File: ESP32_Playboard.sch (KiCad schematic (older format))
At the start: 31 parts

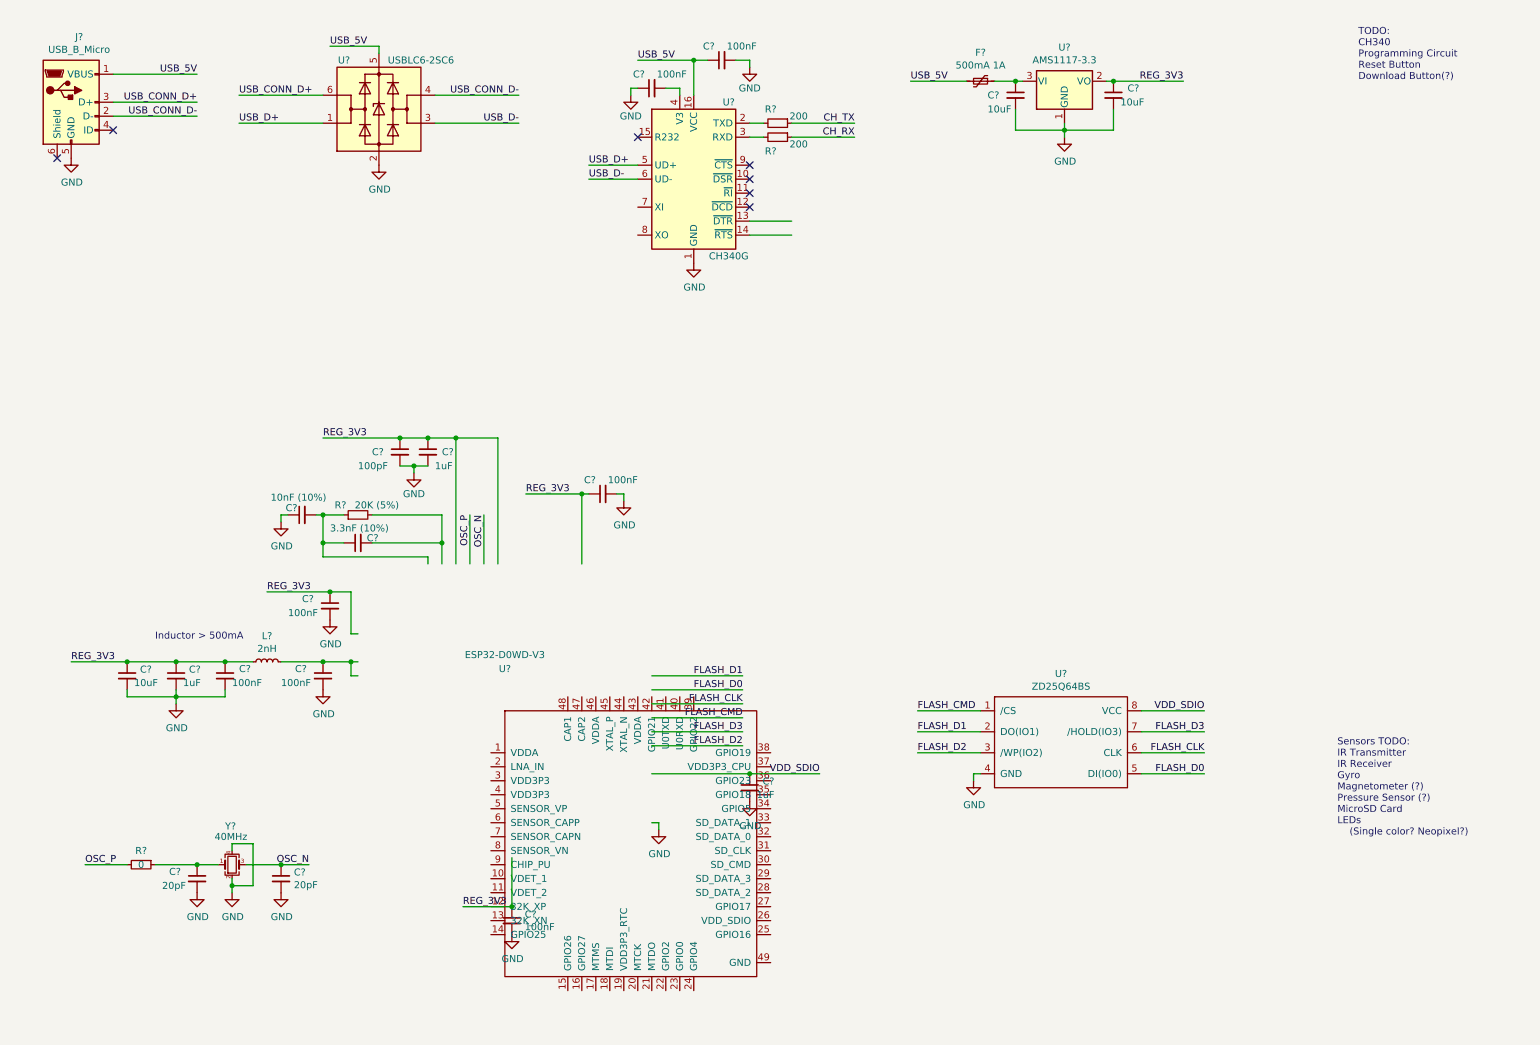
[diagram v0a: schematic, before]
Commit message: Added IR Transmitter & Receiver
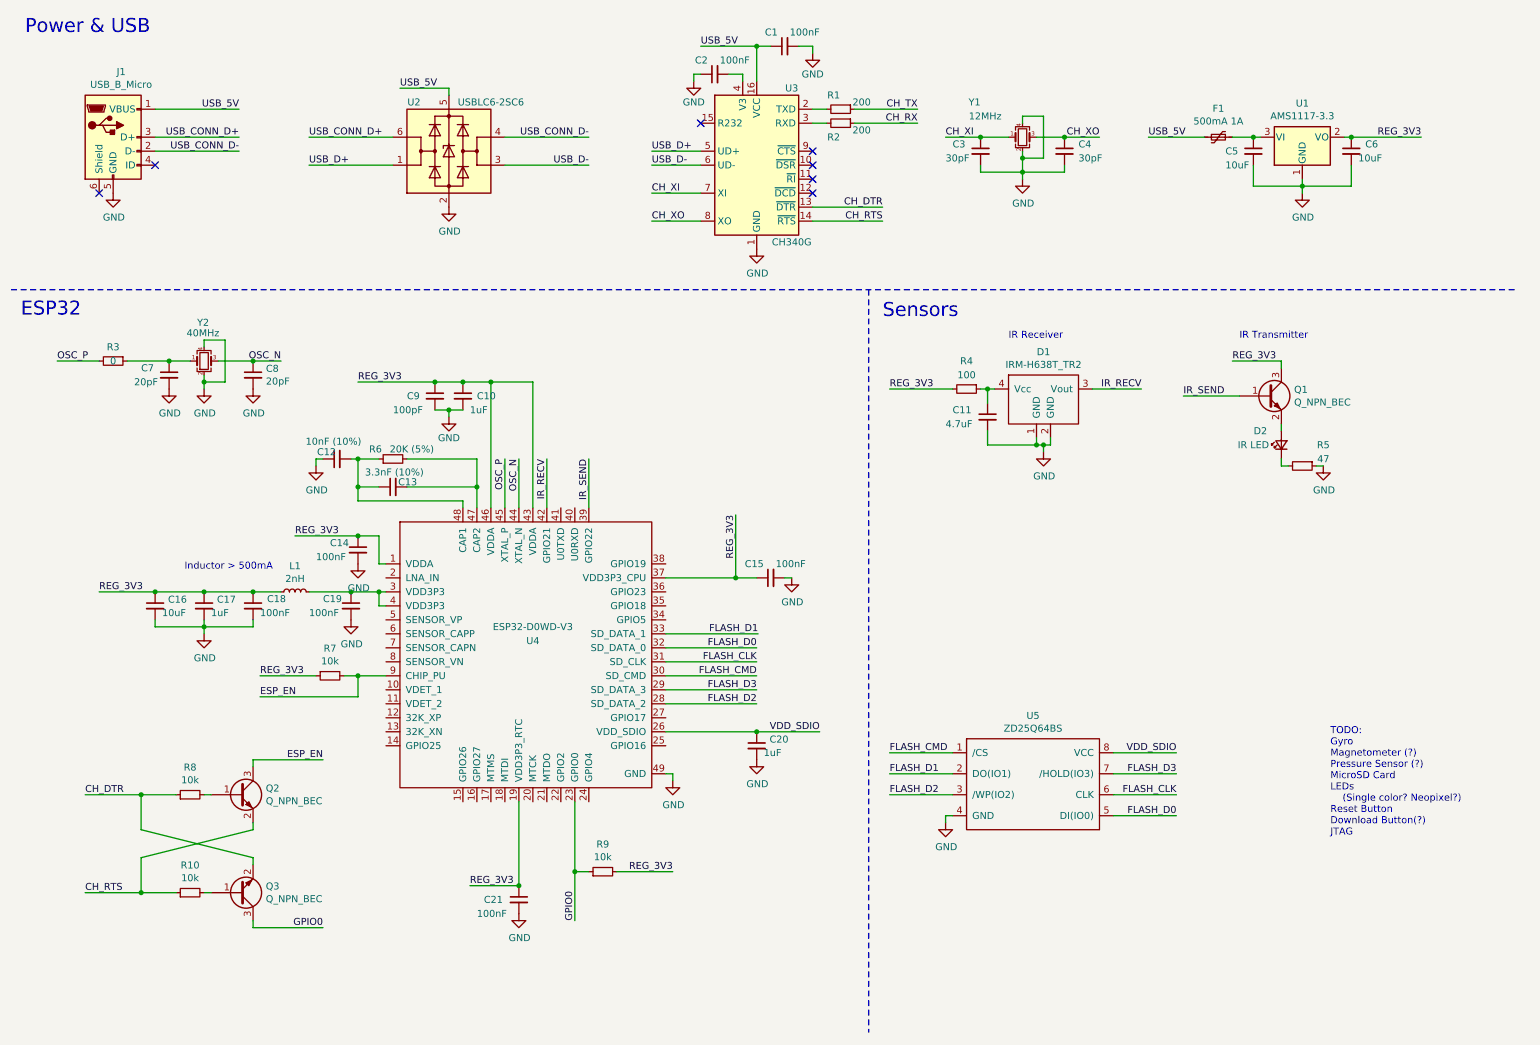
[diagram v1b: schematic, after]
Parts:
- added C11: 4.7uF, Capacitor_SMD:C_0603_1608Metric, symbol Device:C_Small
- added C3, C4: 30pF, Capacitor_SMD:C_0603_1608Metric, symbol Device:C_Small
- added D1: IRM-H638T_TR2, PlayboardLib:LED_SMD-4, symbol PlayboardLib:IRM-H638T_TR2
- added D2: IR LED, LED_SMD:LED_0603_1608Metric, symbol Device:LED_Small
- added Q1, Q2, Q3: Q_NPN_BEC, Package_TO_SOT_SMD:SOT-23, symbol Device:Q_NPN_BEC
- added R10, R7, R8, R9: 10k, Resistor_SMD:R_0603_1608Metric, symbol Device:R_Small
- added R4: 100, Resistor_SMD:R_0603_1608Metric, symbol Device:R_Small
- added R5: 47, Resistor_SMD:R_0603_1608Metric, symbol Device:R_Small
- added Y1: 12MHz, Crystal:Crystal_SMD_3225-4Pin_3.2x2.5mm, symbol Device:Crystal_GND24_Small
- C7, C8: renamed from C?; LCSC Link https://www.lcsc.com/product-detail/C326779.html -> https://www.lcsc.com/product-detail/C105621.html; LCSC Part Number C326779 -> C105621; Manufacturer Part Number CC0603FRNPO9BN200 -> CC0603JRNPO9BN200
- R1, R2: renamed from R?; footprint (none) -> Resistor_SMD:R_0603_1608Metric; LCSC Link (none) -> https://www.lcsc.com/product-detail/C25217.html; LCSC Part Number (none) -> C25217; Manufacturer (none) -> UNI-ROYAL(Uniroyal Elec); Manufacturer Part Number (none) -> 0603WAJ0201T5E
- U3: renamed from U?; LCSC Link (none) -> https://www.lcsc.com/product-detail/C14267.html; LCSC Part Number (none) -> C14267; Manufacturer (none) -> WCH(Jiangsu Qin Heng); Manufacturer Part Number (none) -> CH340G
- gave numbers to parts that had none: 26
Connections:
- net labels added: CH_DTR, CH_RTS, CH_XI, CH_XO, ESP_EN, GPIO0, IR_RECV, IR_SEND
- wire segments 117 -> 179
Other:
- note added: "ESP32"
- note added: "IR Receiver"
- note added: "IR Transmitter"
- note added: "Power & USB"
- note added: "Sensors"
- note added: "TODO:\nGyro\nMagnetometer (?)\nPressure Sensor (?)\nMicroSD Card\nLEDs\n (Single color? Neopixel?)\nReset Button\nDownload Button(?)\nJTAG\n"
- note removed: "Sensors TODO:\nIR Transmitter\nIR Receiver\nGyro\nMagnetometer (?)\nPressure Sensor (?)\nMicroSD Card\nLEDs\n (Single color? Neopixel?)\n"
- note removed: "TODO:\nCH340\nProgramming Circuit\nReset Button\nDownload Button(?)"
- moved on the sheet: C1, C10, C12, C13, C14, C15, C16, C17, C18, C19, C2, C20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

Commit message: Finished adding SD Card, IMU, Temp sensor
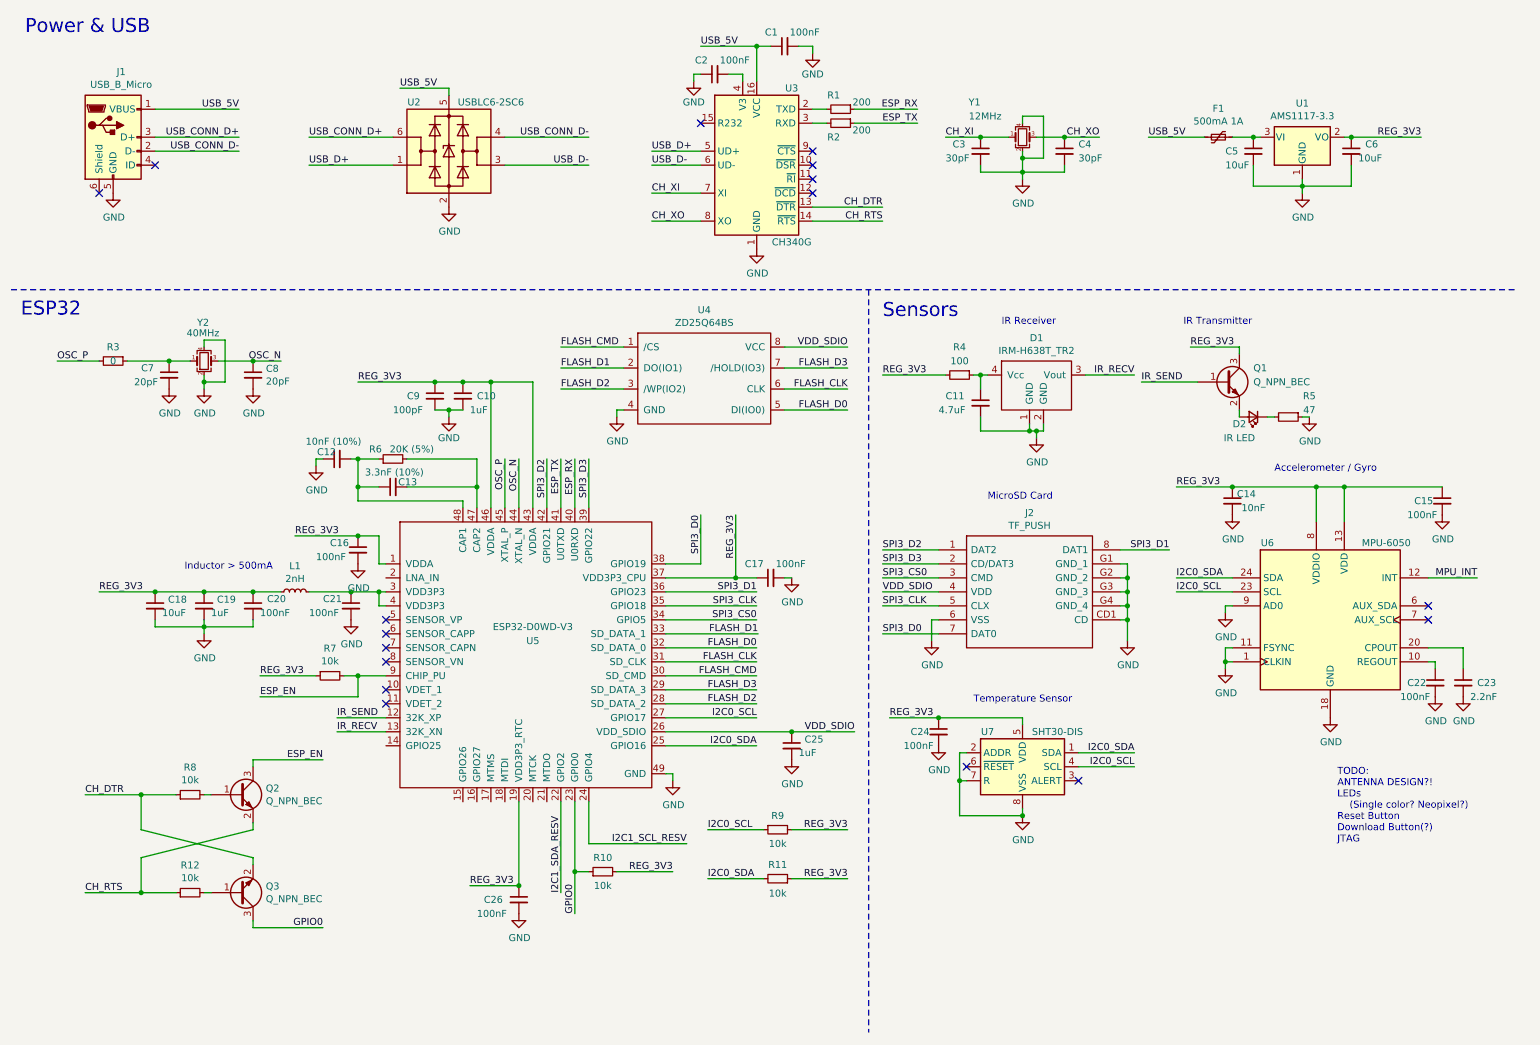
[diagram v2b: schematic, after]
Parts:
- added C14: 10nF, Capacitor_SMD:C_0603_1608Metric, symbol Device:C_Small
- added C15, C22, C24: 100nF, Capacitor_SMD:C_0603_1608Metric, symbol Device:C_Small
- added C23: 2.2nF, Capacitor_SMD:C_0603_1608Metric, symbol Device:C_Small
- added J2: TF_PUSH, PlayboardLib:TFPUSH, symbol PlayboardLib:TF_PUSH
- added R11, R9: 10k, Resistor_SMD:R_0603_1608Metric, symbol Device:R_Small
- added U6: MPU-6050, Sensor_Motion:InvenSense_QFN-24_4x4mm_P0.5mm, symbol Sensor_Motion:MPU-6050
- added U7: SHT30-DIS, Sensor_Humidity:Sensirion_DFN-8-1EP_2.5x2.5mm_P0.5mm_EP1.1x1.7mm, symbol Sensor_Humidity:SHT30-DIS
- C12: LCSC Link https://www.lcsc.com/product-detail/C19702.html -> (none); LCSC Part Number C19702 -> (none); Manufacturer Samsung Electro-Mechanics -> (none); Manufacturer Part Number CL10A106KP8NNNC -> (none)
- renumbered C14 to C16, C15 to C17, C16 to C18, C17 to C19, C18 to C20, C19 to C21, C20 to C25, C21 to C26, R9 to R10, R10 to R12, U5 to U4, U4 to U5
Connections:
- net CH_RX is gone; now on net ESP_TX: R2.1
- net CH_TX is gone; now on net ESP_RX: R1.1
- net GND: now also C14.2, C15.2, C22.2, C23.2, C24.2, J2.6 (VSS), J2.CD1 (CD), J2.G1 (GND_1), J2.G2 (GND_2), J2.G3 (GND_3), J2.G4 (GND_4), U6.1 (CLKIN), U6.11 (FSYNC), U6.18 (GND), U6.9 (AD0), U7.2 (ADDR), U7.7 (R), U7.8 (VSS), U7.9 (VSS)
- net IR_RECV: now also U5.13 (32K_XN); no longer U5.42 (GPIO21)
- net IR_SEND: now also U5.12 (32K_XP); no longer U5.39 (GPIO22)
- net REG_3V3: now also C14.1, C15.1, C24.1, R11.1, R9.2, U6.13 (VDD), U6.8 (VDDIO), U7.5 (VDD)
- net VDD_SDIO: now also J2.4 (VDD)
- net I2C1_SDA_RESV: now reaches U5.22 (GPIO2)
- net I2C1_SCL_RESV: now reaches U5.24 (GPIO4)
- net I2C0_SDA: now reaches U5.25 (GPIO16)
- net I2C0_SDA: now also R11.2, U6.24 (SDA), U7.1 (SDA)
- net I2C0_SCL: now reaches U5.27 (GPIO17)
- net I2C0_SCL: now also R9.1, U6.23 (SCL), U7.4 (SCL)
- net SPI3_CS0: now reaches U5.34 (GPIO5)
- net SPI3_CS0: now also J2.3 (CMD)
- net SPI3_CLK: now reaches U5.35 (GPIO18)
- net SPI3_CLK: now also J2.5 (CLX)
- net SPI3_D1: now reaches U5.36 (GPIO23)
- net SPI3_D1: now also J2.8 (DAT1)
- net SPI3_D0: now reaches U5.38 (GPIO19)
- net SPI3_D0: now also J2.7 (DAT0)
- net ESP_RX: now reaches U5.40 (U0RXD)
- net ESP_TX: now reaches U5.41 (U0TXD)
- new net: C22.1, U6.10 (REGOUT)
- new net: C23.1, U6.20 (CPOUT)
- new net MPU_INT: U6.12 (INT)
- new net SPI3_D2: J2.1 (DAT2), U5.42 (GPIO21)
- new net SPI3_D3: J2.2 (CD/DAT3), U5.39 (GPIO22)
- no-connect marks 7 -> 17
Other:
- note added: "Accelerometer / Gyro"
- note added: "MicroSD Card"
- note added: "TODO:\nANTENNA DESIGN?!\nLEDs\n (Single color? Neopixel?)\nReset Button\nDownload Button(?)\nJTAG\n"
- note added: "Temperature Sensor"
- note removed: "TODO:\nGyro\nMagnetometer (?)\nPressure Sensor (?)\nMicroSD Card\nLEDs\n (Single color? Neopixel?)\nReset Button\nDownload Button(?)\nJTAG\n"
- moved on the sheet: C11, C25, D1, D2, Q1, R4, R5, U4

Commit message: Started work on PCB
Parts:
- added SW1, SW2: SW_SPST, PlayboardLib:TS-1101-C-W, symbol Switch:SW_SPST
- C12: LCSC Link (none) -> https://www.lcsc.com/product-detail/C106218.html; LCSC Part Number (none) -> C106218; Manufacturer (none) -> YAGEO; Manufacturer Part Number (none) -> CC0603KRX7R9BB472
- C14: LCSC Link (none) -> https://www.lcsc.com/product-detail/C57112.html; LCSC Part Number (none) -> C57112; Manufacturer (none) -> FH(Guangdong Fenghua Advanced Tech); Manufacturer Part Number (none) -> 0603B103K500NT
- C23: LCSC Link (none) -> https://www.lcsc.com/product-detail/C1604.html; LCSC Part Number (none) -> C1604; Manufacturer (none) -> FH(Guangdong Fenghua Advanced Tech); Manufacturer Part Number (none) -> 0603B222K500NT
- U7: LCSC Link (none) -> https://www.lcsc.com/product-detail/C77361.html; LCSC Part Number (none) -> C77361; Manufacturer (none) -> Sensirion; Manufacturer Part Number (none) -> SHT30-DIS-B2.5KS
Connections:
- net ESP_EN: now also SW1.2 (B)
- net GND: now also SW1.1 (A), SW2.2 (B)
- net GPIO0: now also SW2.1 (A)
- no-connect marks 17 -> 28
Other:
- note added: "TODO:\nANTENNA DESIGN?!\nLEDs\n (Single color? Neopixel?)\nReset Button\nDownload Button(?)\nJTAG\nREADME"
- note removed: "TODO:\nANTENNA DESIGN?!\nLEDs\n (Single color? Neopixel?)\nReset Button\nDownload Button(?)\nJTAG\n"
- moved on the sheet: Q2, Q3, R12, R7, R8

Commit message: Worked more on PCB layout
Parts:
- removed R3: 0, Resistor_SMD:R_0603_1608Metric, symbol Device:R_Small
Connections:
- net OSC_P is gone; now on net OSC+: U5.45 (XTAL_P)
- net OSC+: now reaches C7.1, Y2.1
- net OSC_N renamed OSC-
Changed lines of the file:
@@
 	1850 3100 1850 3150
 Connection ~ 1850 3150
-Text Label 800  3000 0    50   ~ 0
-OSC_P
-Text Label 2400 3000 2    50   ~ 0
-OSC_N
-Wire Wire Line
-	800  3000 1100 3000
+Text Label 1100 3000 0    50   ~ 0
+OSC+
+Text Label 2500 3000 2    50   ~ 0
+OSC-
 Wire Wire Line
 	1950 3000 2200 3000
-$Comp
-L Device:R_Small R3
-U 1 1 61C94EE5
-P 1200 3000
-F 0 "R3" V 1100 3000 50  0000 C CNN
-F 1 "0" V 1300 3000 50  0000 C CNN
-F 2 "Resistor_SMD:R_0603_1608Metric" H 1200 3000 50  0001 C CNN
-F 3 "~" H 1200 3000 50  0001 C CNN
-F 4 "https://www.lcsc.com/product-detail/C15402.html" H 1200 3000 50  0001 C CNN "LCSC Link"
-F 5 "C15402" H 1200 3000 50  0001 C CNN "LCSC Part Number"
-F 6 "UNI-ROYAL(Uniroyal Elec)" H 1200 3000 50  0001 C CNN "Manufacturer"
-F 7 "0603WAJ0000T5E" H 1200 3000 50  0001 C CNN "Manufacturer Part Number"
-	1    1200 3000
-	0    1    1    0
-$EndComp
 $Comp
 L Device:C_Small C7
@@
 Connection ~ 2200 3000
 Wire Wire Line
-	2200 3000 2400 3000
+	2200 3000 2500 3000
 Connection ~ 1600 3000
 Wire Wire Line
 	1600 3000 1750 3000
-Wire Wire Line
-	1300 3000 1600 3000
 $Comp
 L power:GND #PWR08
@@
 	3600 3350 3600 3400
 Text Label 4100 3700 3    50   ~ 0
-OSC_N
+OSC-
 Text Label 4000 3700 3    50   ~ 0
-OSC_P
+OSC+
 Wire Wire Line
 	4100 4050 4100 3700
@@
 	1    0    0    -1
 $EndComp
+Wire Wire Line
+	1100 3000 1600 3000
 $EndSCHEMATC

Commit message: Finished PCB design
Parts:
- added C14: 2pF, Capacitor_SMD:C_0603_1608Metric, symbol Device:C_Small
- added C15: 2.7pF, Capacitor_SMD:C_0603_1608Metric, symbol Device:C_Small
- added L1: 2.7mH, Inductor_SMD:L_0603_1608Metric, symbol Device:L_Small
- added U5: PCB_ANT, PlayboardLib:ESPRESSIF_ESP32_MIFA_2.4GHz_Right, symbol PlayboardLib:PCB_ANT
- renumbered C14 to C16, C15 to C17, C16 to C18, C17 to C19, C18 to C20, C19 to C21, C20 to C22, C21 to C23, C22 to C24, C23 to C25, C24 to C26, C25 to C27, C26 to C28, L1 to L2, R11 to R10, R12 to R11, R4 to R3, R5 to R4, R6 to R5, R7 to R6, R8 to R7, R9 to R8, R10 to R9, U5 to U6, U6 to U7, U7 to U8
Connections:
- net GND: now also C14.2, C15.2, U5.2
- net ANT: now reaches U6.2 (LNA_IN)
- net ANT: now also C15.1, L1.2
- new net: C14.1, L1.1, U5.1
- no-connect marks 28 -> 27
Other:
- moved on the sheet: C18

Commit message: Began work converting to esp module
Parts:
- removed C10, C21, C27: 1uF, Capacitor_SMD:C_0603_1608Metric, symbol Device:C_Small
- removed C12: 10nF (10%), Capacitor_SMD:C_0603_1608Metric, symbol Device:C_Small
- removed C13: 3.3nF (10%), Capacitor_SMD:C_0603_1608Metric, symbol Device:C_Small
- removed C14: 2pF, Capacitor_SMD:C_0603_1608Metric, symbol Device:C_Small
- removed C15: 2.7pF, Capacitor_SMD:C_0603_1608Metric, symbol Device:C_Small
- removed C18, C19, C22, C23, C28: 100nF, Capacitor_SMD:C_0603_1608Metric, symbol Device:C_Small
- removed C20: 10uF, Capacitor_SMD:C_0603_1608Metric, symbol Device:C_Small
- removed C7, C8: 20pF, Capacitor_SMD:C_0603_1608Metric, symbol Device:C_Small
- removed C9: 100pF, Capacitor_SMD:C_0603_1608Metric, symbol Device:C_Small
- removed L1: 2.7mH, Inductor_SMD:L_0603_1608Metric, symbol Device:L_Small
- removed L2: 2nH, Inductor_SMD:L_0402_1005Metric, symbol Device:L_Small
- removed R5: 20K (5%), Resistor_SMD:R_0603_1608Metric, symbol Device:R_Small
- removed R6, R9: 10k, Resistor_SMD:R_0603_1608Metric, symbol Device:R_Small
- removed U4: ZD25Q64BS, Package_SO:SOP-8_5.28x5.23mm_P1.27mm, symbol PlayboardLib:ZD25Q64BS
- removed U5: PCB_ANT, PlayboardLib:ESPRESSIF_ESP32_MIFA_2.4GHz_Right, symbol PlayboardLib:PCB_ANT
- removed U6: ESP32-D0WD-V3, Package_DFN_QFN:QFN-48-1EP_5x5mm_P0.35mm_EP3.7x3.7mm_ThermalVias, symbol PlayboardLib:ESP32-D0WD-V3
- removed Y2: 40MHz, Crystal:Crystal_SMD_3225-4Pin_3.2x2.5mm, symbol Device:Crystal_GND24_Small
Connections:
- net VDD_SDIO is gone; now on net REG_3V3: J2.4 (VDD)
- net ESP_EN: no longer SW1.2 (B)
- net GND: no longer SW1.1 (A), SW2.2 (B)
- net GPIO0: no longer SW2.1 (A)
- no-connect marks 27 -> 12
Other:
- note removed: "Inductor > 500mA"
- moved on the sheet: Q2, Q3, R10, R11, R7, R8, SW1, SW2

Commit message: Updated schematic to include wrover module
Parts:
- added C8: 22uF, Capacitor_SMD:C_0603_1608Metric, symbol Device:C_Small
- added C9: 100nF, Capacitor_SMD:C_0603_1608Metric, symbol Device:C_Small
- added R5: 10k, Resistor_SMD:R_0603_1608Metric, symbol Device:R_Small
- added U4: ESP32-WROVER-I, PlayboardLib:XCVR_ESP32-WROVER-I, symbol PlayboardLib:ESP32-WROVER-I
- renumbered C16 to C10, C17 to C11, C24 to C12, C25 to C13, C26 to C14, C11 to C7, R7 to R6, R8 to R7, R11 to R8, R10 to R9, U7 to U5, U8 to U6
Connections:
- net ESP_EN is gone; now on net RESET: Q2.3 (C)
- net ESP_RX: now also U4.34 (RXD0)
- net ESP_TX: now also U4.35 (TXD0)
- net GND: now also SW1.2 (B), SW2.2 (B), C8.1, C9.1, U4.1 (GND), U4.15 (GND), U4.38 (GND), U4.39 (EXP)
- net GPIO0: now also SW2.1 (A), U4.25 (IO0)
- net I2C0_SCL: now also U4.26 (IO4)
- net I2C0_SDA: now also U4.24 (IO2)
- net IR_RECV: now also U4.6 (IO34)
- net IR_SEND: now also U4.8 (IO32)
- net REG_3V3: now also C8.2, C9.2, R5.1, U4.2 (VDD3V3)
- net SPI3_CLK: now also U4.30 (IO18)
- net SPI3_CS0: now also U4.29 (IO5)
- net SPI3_D0: now also U4.31 (IO19)
- net SPI3_D1: now also U4.37 (IO23)
- net SPI3_D2: now also U4.33 (IO21)
- net SPI3_D3: now also U4.36 (IO22)
- net RESET: now reaches SW1.1 (A)
- net RESET: now also R5.2, U4.3 (EN)
- no-connect marks 12 -> 23
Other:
- note added: "TODO:\nLEDs\n (Single color? Neopixel?)\nReset Button\nDownload Button(?)\nJTAG\nREADME"
- note removed: "TODO:\nANTENNA DESIGN?!\nLEDs\n (Single color? Neopixel?)\nReset Button\nDownload Button(?)\nJTAG\nREADME"
- moved on the sheet: SW1, SW2
